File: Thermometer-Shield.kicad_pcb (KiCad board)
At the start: 2 copper layers, 51 parts, among them J1 TempSensor, J10 Out-A, J11 Out-B, J12 Out-C, J13 Out-D, J14 Pin12, J2 Shift-A, J3 Shift-B, J4 Analog, J5 I2C, J6 Pin9, J7 Trig-G, J8 Trig-H, J9 Outputs, Q1 Q_PNP_BCE, Q2 Q_PNP_BCE, Q3 Q_PNP_BCE, Q4 Q_PNP_BCE, SW1 SW_SPST, SW2 SW_SPST, SW3 SW_SPST, SW4 SW_SPST, U1 74HC595, U2 74HC595, U3 ULN2803A

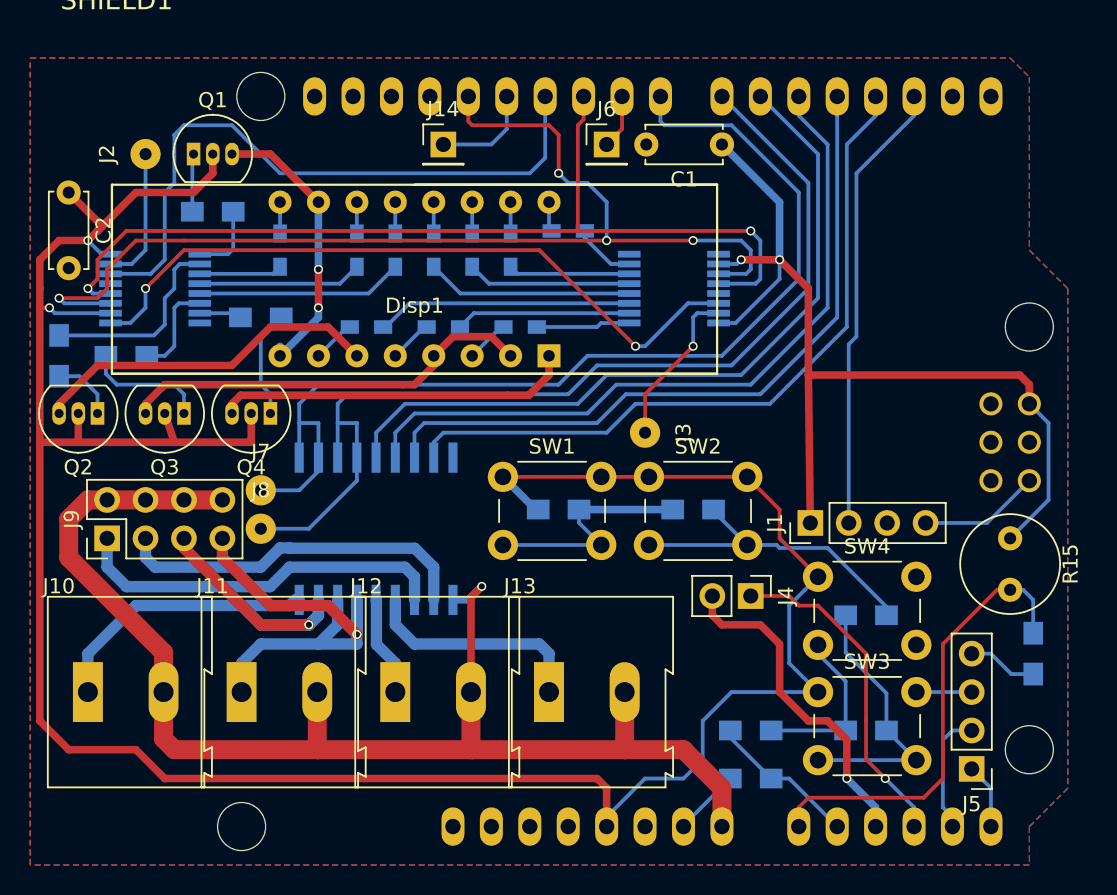
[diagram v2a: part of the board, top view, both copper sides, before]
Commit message: increased trace widths for etching
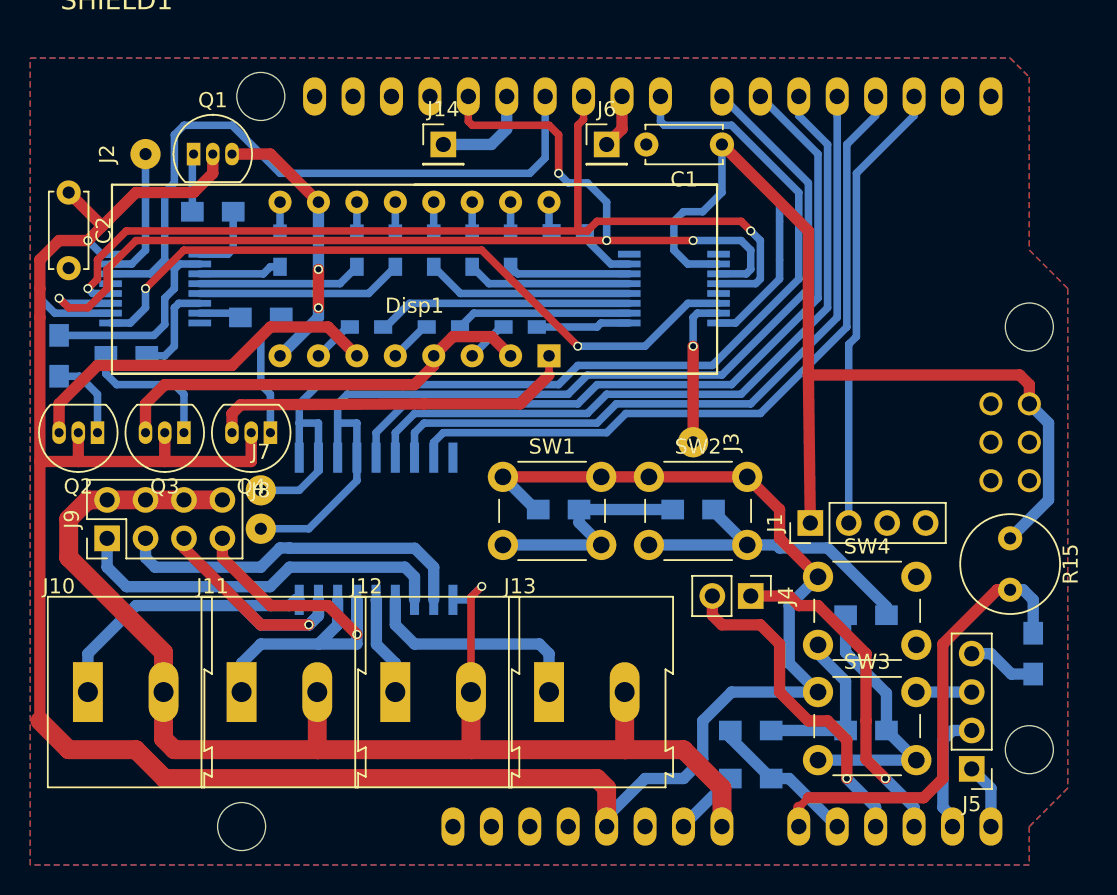
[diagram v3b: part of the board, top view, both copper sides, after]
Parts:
- moved J3 3.24 mm to (192.4, 77.5)
- moved Q2 1.27 mm to (153.0, 76.8)
- moved Q3 1.27 mm to (158.8, 76.8)
- moved Q4 1.27 mm to (164.5, 76.8)
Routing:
- net VCC: track 242.5 -> 265.1 mm, vias 4 -> 1
- net GND: track 17.1 -> 9.08 mm
- net Net-(Q3-Pad1): track 8.18 -> 9.45 mm
- net Net-(Q2-Pad1): track 4.30 -> 5.57 mm
- net Dig3: track 27.5 -> 28.8 mm
- net Dig2: track 23.2 -> 24.5 mm
- net Net-(J6-Pad1): track 4.48 -> 3.60 mm
- net Dig4: track 23.6 -> 24.5 mm
- net Net-(J3-Pad1): track 10.7 -> 10.1 mm
- net Net-(Q4-Pad1): track 7.22 -> 7.85 mm
- net Dig1: track 18.9 -> 18.2 mm
- net SCK: track 72.7 -> 73.2 mm
- net SS: track 63.9 -> 64.4 mm
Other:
- net class Default: clearance 0.2 -> 0.1; trace_width 0.25 -> 0.5
- net class Dig-Anode: clearance 0.2 -> 0.1
- rule trace_clearance: 0.2 -> 0.1

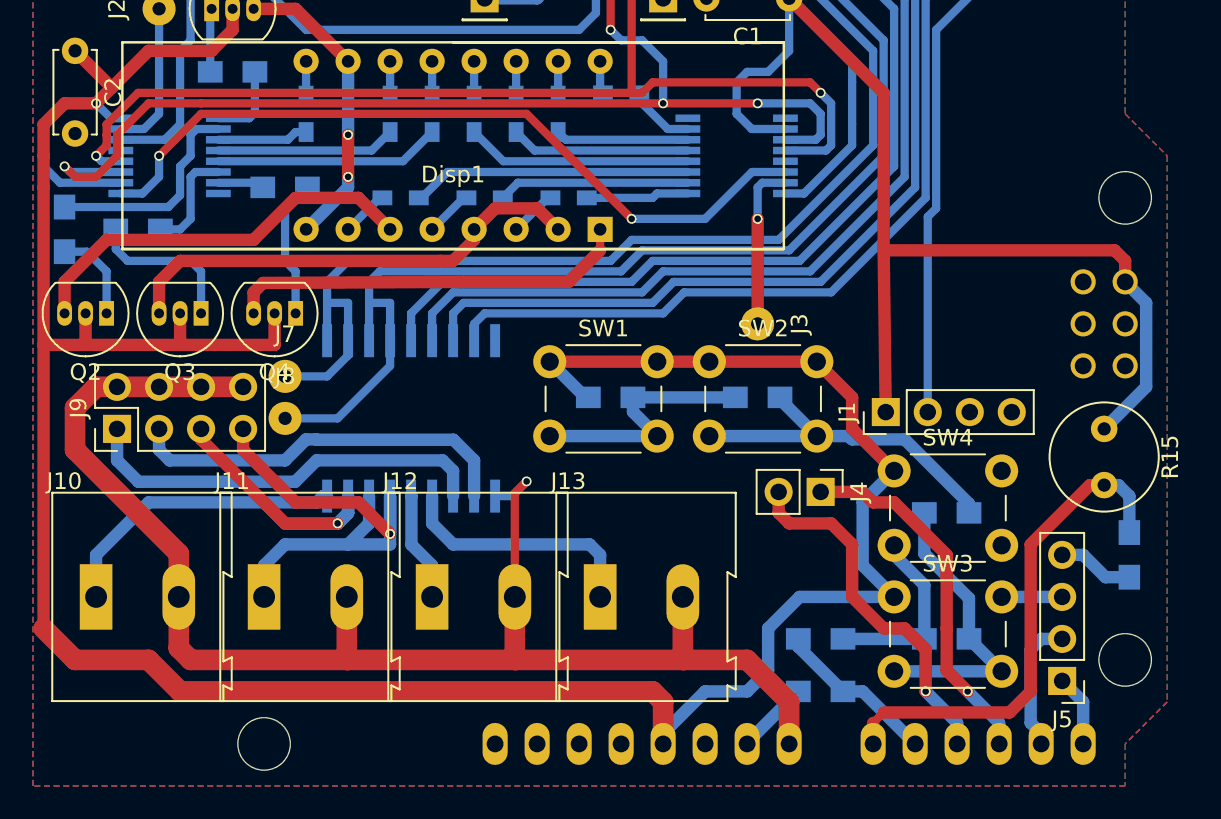
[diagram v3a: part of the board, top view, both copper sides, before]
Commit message: minor trace tweaks
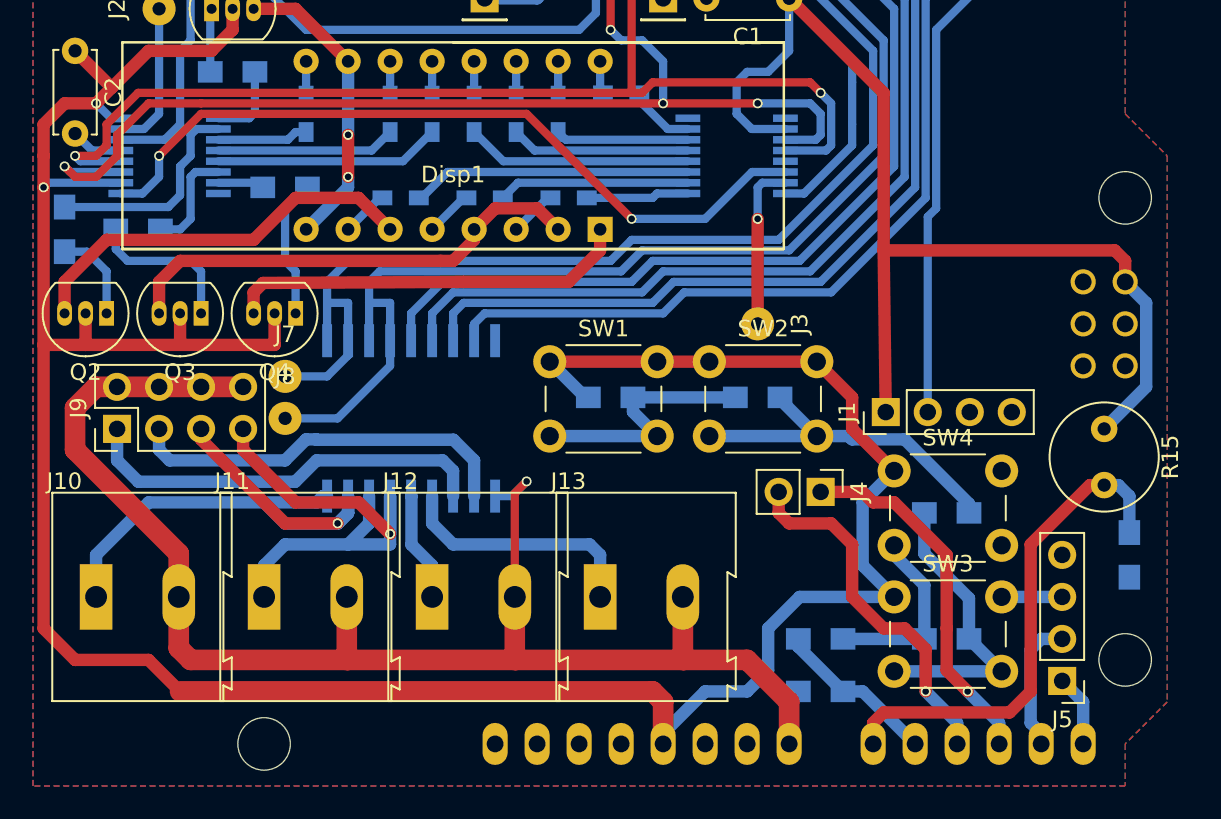
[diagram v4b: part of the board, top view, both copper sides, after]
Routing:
- net VCC: track 265.1 -> 258.6 mm, vias 1 -> 2
- net GND: track 9.08 -> 3.27 mm
- net SS: track 64.4 -> 67.0 mm
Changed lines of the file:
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@@
   (general
     (links 131)
-    (no_connects 10)
+    (no_connects 5)
     (area 147.003095 46.5408 218.735 106.16)
     (thickness 1.6)
     (drawings 0)
-    (tracks 485)
+    (tracks 481)
     (zones 0)
     (modules 51)
@@
   (layers
     (0 F.Cu signal)
-    (31 B.Cu signal)
+    (31 B.Cu signal hide)
     (32 B.Adhes user)
     (33 F.Adhes user)
@@
     (user_trace_width 1.25)
     (trace_clearance 0.1)
-    (zone_clearance 0.508)
+    (zone_clearance 0.254)
     (zone_45_only no)
     (trace_min 0.2)
@@
   (segment (start 162.494998 74.995002) (end 161.925 75.565) (width 0.75) (layer F.Cu) (net 1) (status 20))
   (segment (start 162.494998 74.995002) (end 174.625 74.93) (width 0.75) (layer F.Cu) (net 1))
-  (segment (start 182.88 73.025) (end 182.88 71.755) (width 0.5) (layer F.Cu) (net 1))
+  (segment (start 182.88 73.025) (end 182.88 71.755) (width 0.75) (layer F.Cu) (net 1))
   (segment (start 175.26 71.755) (end 176.53 70.485) (width 0.75) (layer F.Cu) (net 2))
   (segment (start 179.07 70.485) (end 180.34 71.755) (width 0.75) (layer F.Cu) (net 2))
@@
   (segment (start 170.18 76.2) (end 170.18 78.485) (width 0.5) (layer B.Cu) (net 16))
   (segment (start 168.91 76.2) (end 170.18 76.2) (width 0.5) (layer B.Cu) (net 16))
+  (segment (start 153.895 66.985) (end 152.155 66.985) (width 0.5) (layer B.Cu) (net 17))
+  (segment (start 152.155 66.985) (end 151.13 65.96) (width 0.5) (layer B.Cu) (net 17))
   (segment (start 191.77 102.87) (end 191.77 102.79) (width 0.25) (layer B.Cu) (net 17) (status 30))
-  (segment (start 191.77 102.79) (end 194.865 99.695) (width 0.75) (layer B.Cu) (net 17) (status 10))
-  (segment (start 210.82 91.44) (end 212.09 91.44) (width 0.75) (layer B.Cu) (net 17))
-  (segment (start 212.09 91.44) (end 213.44 92.79) (width 0.75) (layer B.Cu) (net 17))
-  (segment (start 213.44 92.79) (end 214.884 92.79) (width 0.75) (layer B.Cu) (net 17))
   (segment (start 207.01 54.61) (end 207.01 55.88) (width 0.5) (layer B.Cu) (net 18))
   (segment (start 207.01 55.88) (end 203.2 59.69) (width 0.5) (layer B.Cu) (net 18))
@@
   (segment (start 167.005 89.554998) (end 163.849998 89.554998) (width 0.75) (layer B.Cu) (net 19))
   (segment (start 167.64 88.919998) (end 167.005 89.554998) (width 0.75) (layer B.Cu) (net 19))
-  (segment (start 149.225 67.945) (end 149.225 65.405) (width 0.5) (layer B.Cu) (net 20))
-  (segment (start 150.215 68.935) (end 149.225 67.945) (width 0.5) (layer B.Cu) (net 20))
-  (segment (start 153.895 68.935) (end 150.215 68.935) (width 0.5) (layer B.Cu) (net 20))
-  (segment (start 150.495 64.135) (end 152.4 64.135) (width 0.5) (layer B.Cu) (net 20))
-  (segment (start 149.225 65.405) (end 150.495 64.135) (width 0.5) (layer B.Cu) (net 20))
+  (segment (start 153.895 68.935) (end 149.505 68.935) (width 0.5) (layer B.Cu) (net 20))
+  (via (at 149.225 69.215) (size 0.6) (drill 0.4) (layers F.Cu B.Cu) (net 20))
+  (segment (start 149.505 68.935) (end 149.225 69.215) (width 0.5) (layer B.Cu) (net 20))
   (segment (start 191.77 62.23) (end 193.04 62.23) (width 0.5) (layer B.Cu) (net 20))
   (segment (start 192.05 65.685) (end 191.135 64.77) (width 0.5) (layer B.Cu) (net 20))
@@
   (segment (start 186.69 100.33) (end 186.055 99.695) (width 1.25) (layer F.Cu) (net 20))
   (segment (start 186.055 99.695) (end 157.48 99.695) (width 1.25) (layer F.Cu) (net 20))
-  (segment (start 157.48 99.695) (end 155.575 97.79) (width 1.25) (layer F.Cu) (net 20))
-  (segment (start 155.575 97.79) (end 151.13 97.79) (width 1.25) (layer F.Cu) (net 20))
-  (segment (start 151.13 97.79) (end 149.225 95.885) (width 1.25) (layer F.Cu) (net 20))
+  (segment (start 157.48 99.695) (end 155.575 97.79) (width 0.75) (layer F.Cu) (net 20))
+  (segment (start 155.575 97.79) (end 151.13 97.79) (width 0.75) (layer F.Cu) (net 20))
+  (segment (start 151.13 97.79) (end 149.225 95.885) (width 0.75) (layer F.Cu) (net 20))
   (segment (start 149.225 95.885) (end 149.225 78.74) (width 0.75) (layer F.Cu) (net 20))
   (segment (start 160.655 59.69) (end 160.655 58.42) (width 0.75) (layer F.Cu) (net 20))
@@
   (segment (start 163.83 70.485) (end 163.83 73.66) (width 0.5) (layer B.Cu) (net 29))
   (segment (start 199.39 102.87) (end 199.39 101.6) (width 0.75) (layer F.Cu) (net 30) (status 30))
-  (segment (start 199.39 101.6) (end 200.025 100.965) (width 0.5) (layer F.Cu) (net 30) (status 10))
+  (segment (start 199.39 101.6) (end 200.025 100.965) (width 0.75) (layer F.Cu) (net 30) (status 10))
   (segment (start 212.5 87.22) (end 213.36 87.22) (width 0.75) (layer F.Cu) (net 30))
   (segment (start 208.915 90.805) (end 212.5 87.22) (width 0.75) (layer F.Cu) (net 30))
@@
   (segment (start 184.785 56.515) (end 184.785 63.5) (width 0.5) (layer F.Cu) (net 50))
   (segment (start 185.166 54.61) (end 185.166 54.991) (width 0.25) (layer F.Cu) (net 50) (status 30))
-  (segment (start 153.035 66.675) (end 152.4 67.31) (width 0.5) (layer F.Cu) (net 50))
+  (segment (start 152.4 67.31) (end 151.13 67.31) (width 0.5) (layer F.Cu) (net 50))
   (segment (start 184.785 63.5) (end 154.94 63.5) (width 0.5) (layer F.Cu) (net 50))
   (segment (start 153.035 65.405) (end 154.94 63.5) (width 0.5) (layer F.Cu) (net 50))
-  (segment (start 153.035 66.04) (end 153.035 65.405) (width 0.5) (layer F.Cu) (net 50))
-  (segment (start 153.035 66.675) (end 153.035 66.04) (width 0.5) (layer F.Cu) (net 50))
-  (segment (start 152.725 67.635) (end 153.895 67.635) (width 0.5) (layer B.Cu) (net 50))
-  (segment (start 152.4 67.31) (end 152.725 67.635) (width 0.5) (layer B.Cu) (net 50))
-  (via (at 152.4 67.31) (size 0.6) (drill 0.4) (layers F.Cu B.Cu) (net 50))
+  (segment (start 153.035 66.675) (end 153.035 65.405) (width 0.5) (layer F.Cu) (net 50))
+  (segment (start 152.4 67.31) (end 153.035 66.675) (width 0.5) (layer F.Cu) (net 50))
+  (segment (start 151.455 67.635) (end 153.895 67.635) (width 0.5) (layer B.Cu) (net 50))
+  (segment (start 151.13 67.31) (end 151.455 67.635) (width 0.5) (layer B.Cu) (net 50))
+  (via (at 151.13 67.31) (size 0.6) (drill 0.4) (layers F.Cu B.Cu) (net 50))
   (segment (start 185.42 54.864) (end 185.166 54.61) (width 0.25) (layer F.Cu) (net 50) (status 30))
   (segment (start 153.895 66.335) (end 156.55 66.335) (width 0.5) (layer B.Cu) (net 51))
@@
   (segment (start 153.67 81.28) (end 156.21 81.28) (width 1.25) (layer F.Cu) (net 66))
   (zone (net 17) (net_name GND) (layer B.Cu) (hatch edge 0.508)
-    (connect_pads (clearance 0.508))
+    (connect_pads (clearance 0.254))
     (min_thickness 0.254)
     (fill yes (arc_segments 16) (thermal_gap 0.508) (thermal_bridge_width 0.508))
@@
   )
   (zone (net 17) (net_name GND) (layer F.Cu) (hatch edge 0.508)
-    (connect_pads (clearance 0.508))
+    (connect_pads (clearance 0.254))
     (min_thickness 0.254)
     (fill yes (arc_segments 16) (thermal_gap 0.508) (thermal_bridge_width 0.508))
